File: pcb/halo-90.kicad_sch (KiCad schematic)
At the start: 111 parts, among them U1 UFQFPN28, U2 LSM6DSM

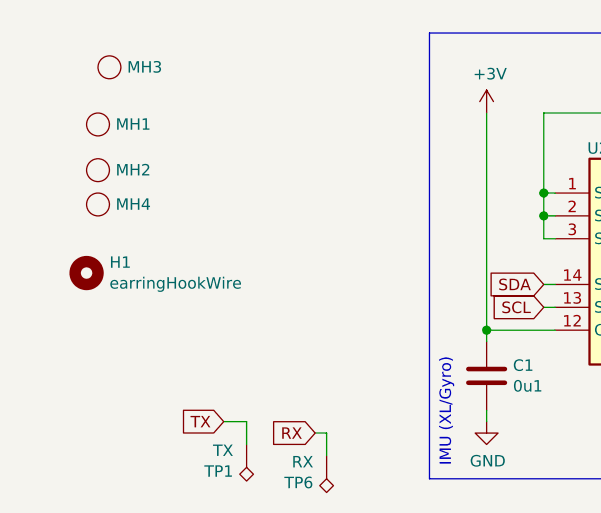
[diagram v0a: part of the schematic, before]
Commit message: Moved earwire andded to docs
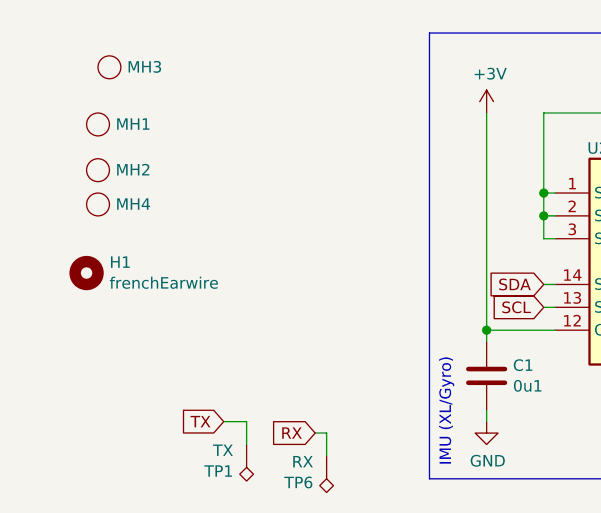
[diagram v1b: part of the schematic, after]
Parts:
- H1: value earringHookWire -> frenchEarwire; footprint earringHookWire:earringHookWire -> frenchEarwire:frenchEarwire
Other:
- title: Halo -> HALO-90

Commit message: Docs improvment
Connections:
- net RX: no longer TP6.1, U1.23 (PC2)
- net TX: no longer TP1.1, U1.24 (PC3)
- new net: TP6.1, U1.23 (PC2)
- new net: TP1.1, U1.24 (PC3)
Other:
- note added: "Chalieplex LEDs"
- note added: "Earwire"
- note added: "Microphone"
- note added: "Tooling"
- moved on the sheet: BT1, C2, H1, MH1, MH2, MH3, MH4, MK1, R1, R2, TP1, TP3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

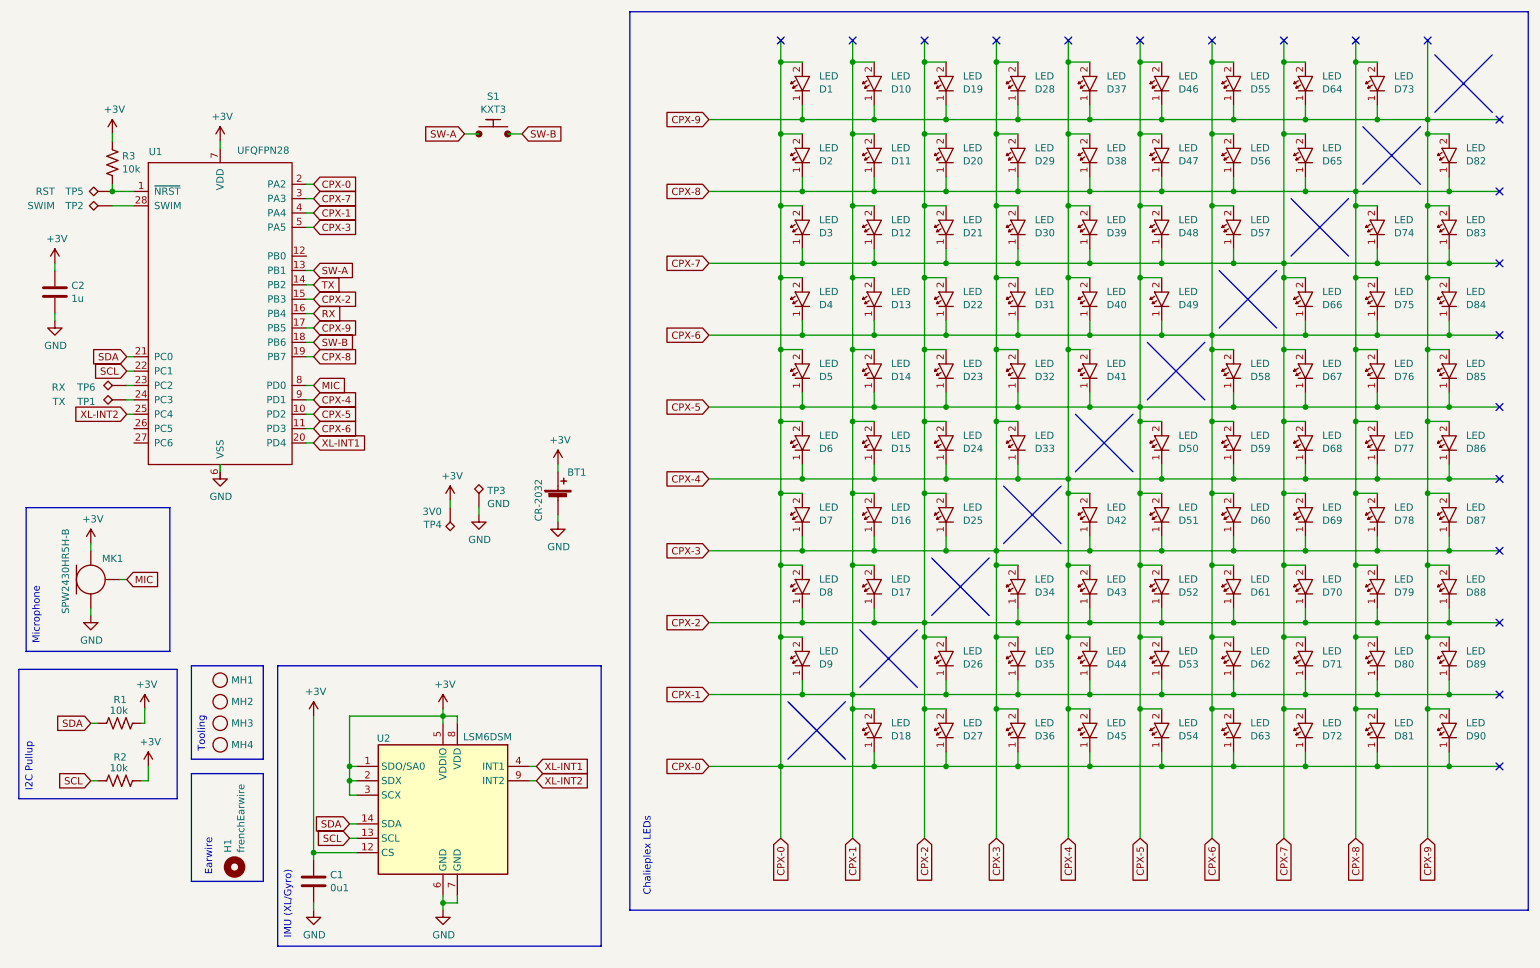
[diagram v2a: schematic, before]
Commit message: Added gifs to readme
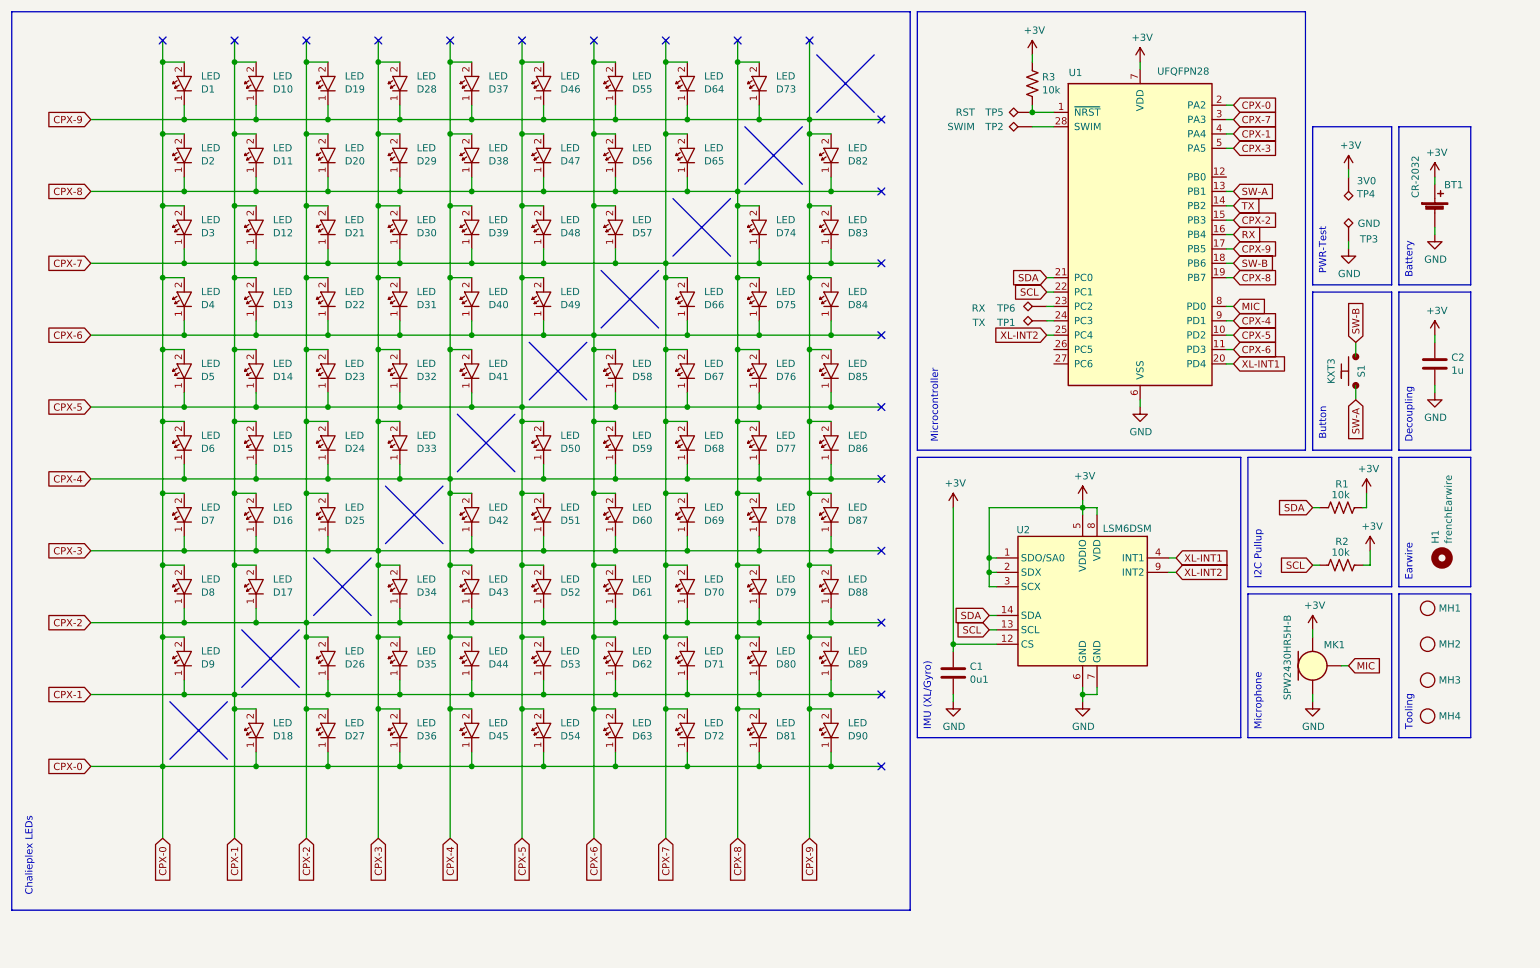
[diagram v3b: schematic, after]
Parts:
- BT1: footprint BAT-HLD-001:BAT-HLD-001-HALO -> BAT-HLD-001:BAT-HLD-001
- H1: symbol earringHookWire:earringHookWire -> frenchEarwire:frenchEarwire
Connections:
- net GND: now also U1.6 (VSS)
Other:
- note added: "Battery"
- note added: "Button"
- note added: "Decoupling"
- note added: "Microcontroller"
- note added: "PWR-Test"
- moved on the sheet: BT1, C1, C2, D1, D10, D11, D12, D13, D14, D15, D16, D17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

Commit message: Acceleometer shcematic done?
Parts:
- removed C1: 0u1, passives:C-0402, symbol passives:C-0402
- removed C2: 1u, passives:C-0402, symbol passives:C-0402
- removed H1: frenchEarwire, frenchEarwire:frenchEarwire, symbol frenchEarwire:frenchEarwire
- removed MH1, MH2, MH3, MH4: toolingHole, tooling:1.152mm-ToolingHole, symbol tooling:toolingHole
- removed MK1: SPW2430HR5H-B, SPW2430HR5H-B:SPW2430HR5H-B, symbol SPW2430HR5H-B:SPW2430HR5H-B
- removed R1, R2, R3: 10k, passives:R-0402, symbol passives:R-0402
- removed S1: KXT3, KXT3:KXT3, symbol KXT3:KXT3
- removed TP1: TX, tooling:TestPoint_Pad_D1.0mm, symbol tooling:TestPoint_D1.0
- removed TP2: SWIM, tooling:TestPoint_Pad_D1.0mm, symbol tooling:TestPoint_D1.0
- removed TP3: GND, tooling:TestPoint_Pad_D1.0mm, symbol tooling:TestPoint_D1.0
- removed TP4: 3V0, tooling:TestPoint_Pad_D1.0mm, symbol tooling:TestPoint_D1.0
- removed TP5: RST, tooling:TestPoint_Pad_D1.0mm, symbol tooling:TestPoint_D1.0
- removed TP6: RX, tooling:TestPoint_Pad_D1.0mm, symbol tooling:TestPoint_D1.0
- removed U1: UFQFPN28, STM8L15xxx:UFQFPN28, symbol STM8L15xxx:UFQFPN28
- removed U2: LSM6DSM, LSM6DSM:LGA-14_3x2.5mm_6-6, symbol LSM6DSM:LSM6DSM
- added C1, C2, C3: 100n, C-0402:C-0402, symbol C-0402:100n
- added H1: SMTSO1610MTJ, SMTSO1610MTJ:SMTSO1610MTJ, symbol SMTSO1610MTJ:SMTSO1610MTJ
- added J1: TC2030-SWIM-NL, TC2030-IDC-NL:Tag-Connect_TC2030-IDC-NL_2x03_P1.27mm_Vertical, symbol TC2030-IDC-NL:TC2030-SWIM-NL
- added R1, R2, R3: 10k, R-0402:R-0402, symbol R-0402:10k
- added U1: STM8L151xxx, STM8L15xxx:UFQFPN28, symbol STM8L15xxx:STM8L151xxx
- added U2: SC7A20HTR, SC7A20HTR:SC7A20HTR, symbol SC7A20HTR:SC7A20HTR
- added U3: DRV5032, DRV5032:DRV5032, symbol DRV5032:DRV5032
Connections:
- net +3V: now also C1.1, C2.1, C3.1, J1.1 (VCC), R1.2, R2.2, R3.1, U1.7 (VDD), U2.3 (VDDIO), U2.7 (VDD), U3.1 (VCC)
- net CPX-0: now also U1.2 (PA2)
- net CPX-1: now also U1.4 (PA4)
- net CPX-2: now also U1.15 (PB3)
- net CPX-3: now also U1.5 (PA5)
- net CPX-4: now also U1.9 (PD1)
- net CPX-5: now also U1.10 (PD2)
- net CPX-6: now also U1.11 (PD3)
- net CPX-7: now also U1.3 (PA3)
- net CPX-8: now also U1.19 (PB7)
- net CPX-9: now also U1.17 (PB5)
- net GND: now also C1.2, C2.2, C3.2, J1.5 (GND), U1.6 (VSS), U2.8 (GNDIO), U2.9 (GND), U3.3 (GND)
- net RX: now also J1.3 (RX), U1.23 (PC2)
- net SCL: now also R2.1, U1.22 (PC1), U2.12 (SCx)
- net SDA: now also R1.1, U1.21 (PC0), U2.2 (SDx)
- net TX: now also J1.2 (TX), U1.24 (PC3)
- net XL-INT1: now also U1.20 (PD4), U2.5 (INT1)
- net XL-INT2: now also U1.25 (PC4), U2.6 (INT2)
- new net HALL: U1.8 (PD0), U3.2 (OUT)
- new net SWIM: J1.4 (SWIM), U1.28 (SWIM)
- new net ~{RESET}: J1.6 (~{RESET}), R3.2, U1.1 (~{NRST})
- no-connect marks 20 -> 29
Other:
- note added: "HALL"
- note added: "Programmer"
- note removed: "Button"
- note removed: "Decoupling"
- note removed: "Microphone"
- note removed: "PWR-Test"
- note removed: "Tooling"
- moved on the sheet: BT1

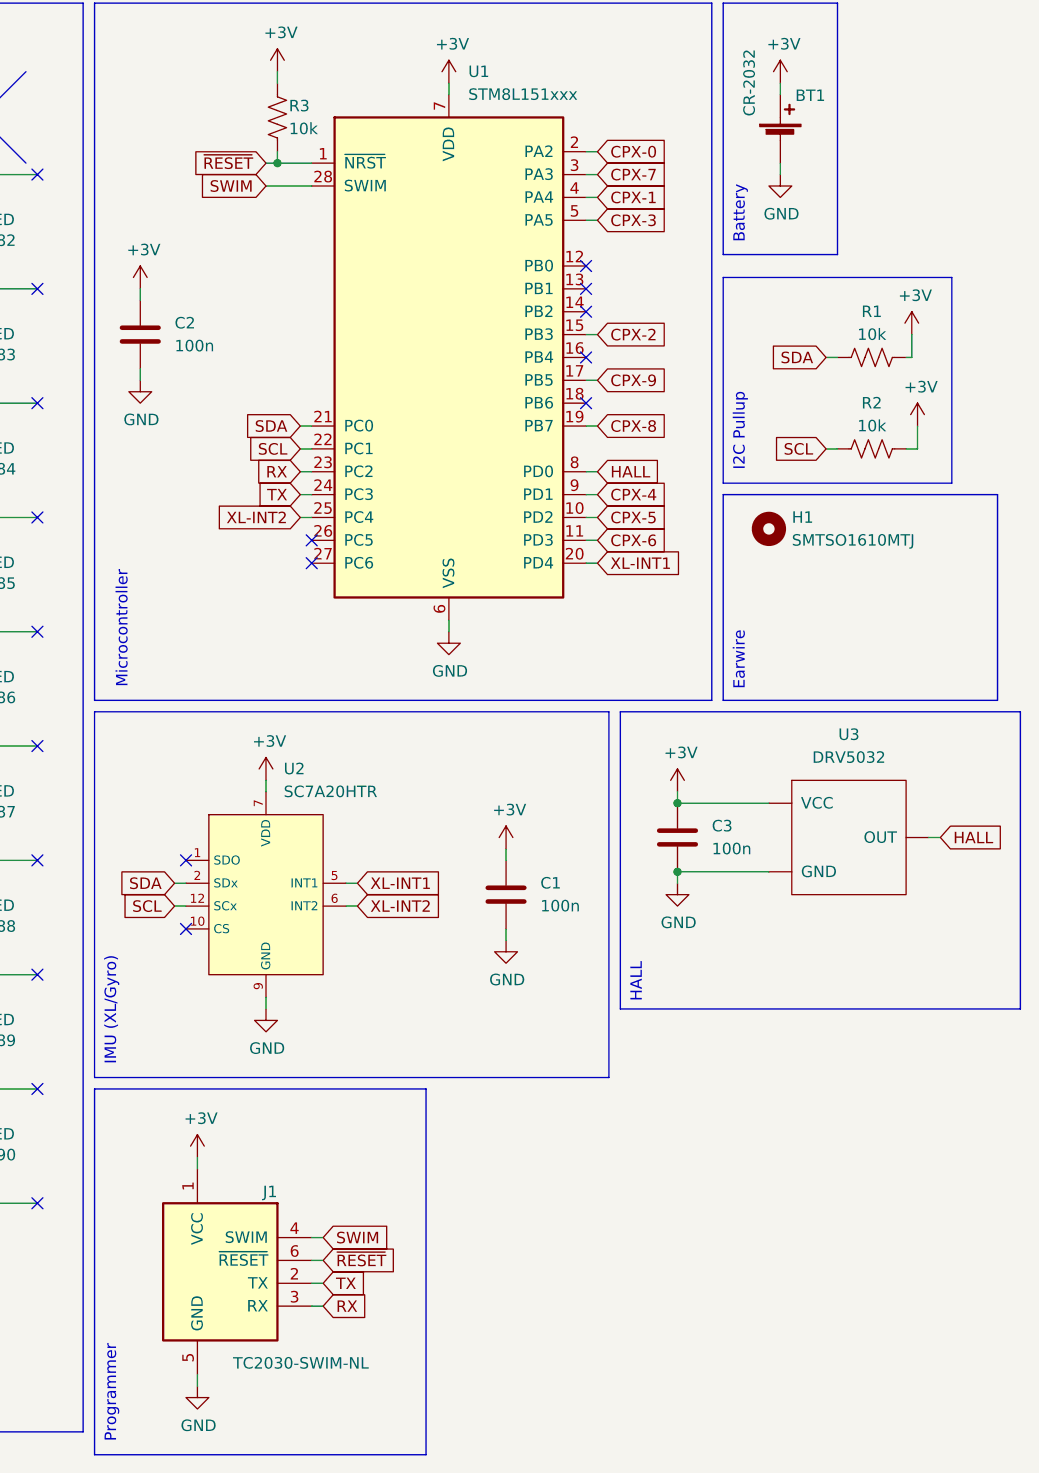
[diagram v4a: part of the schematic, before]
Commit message: updated layout, added cover
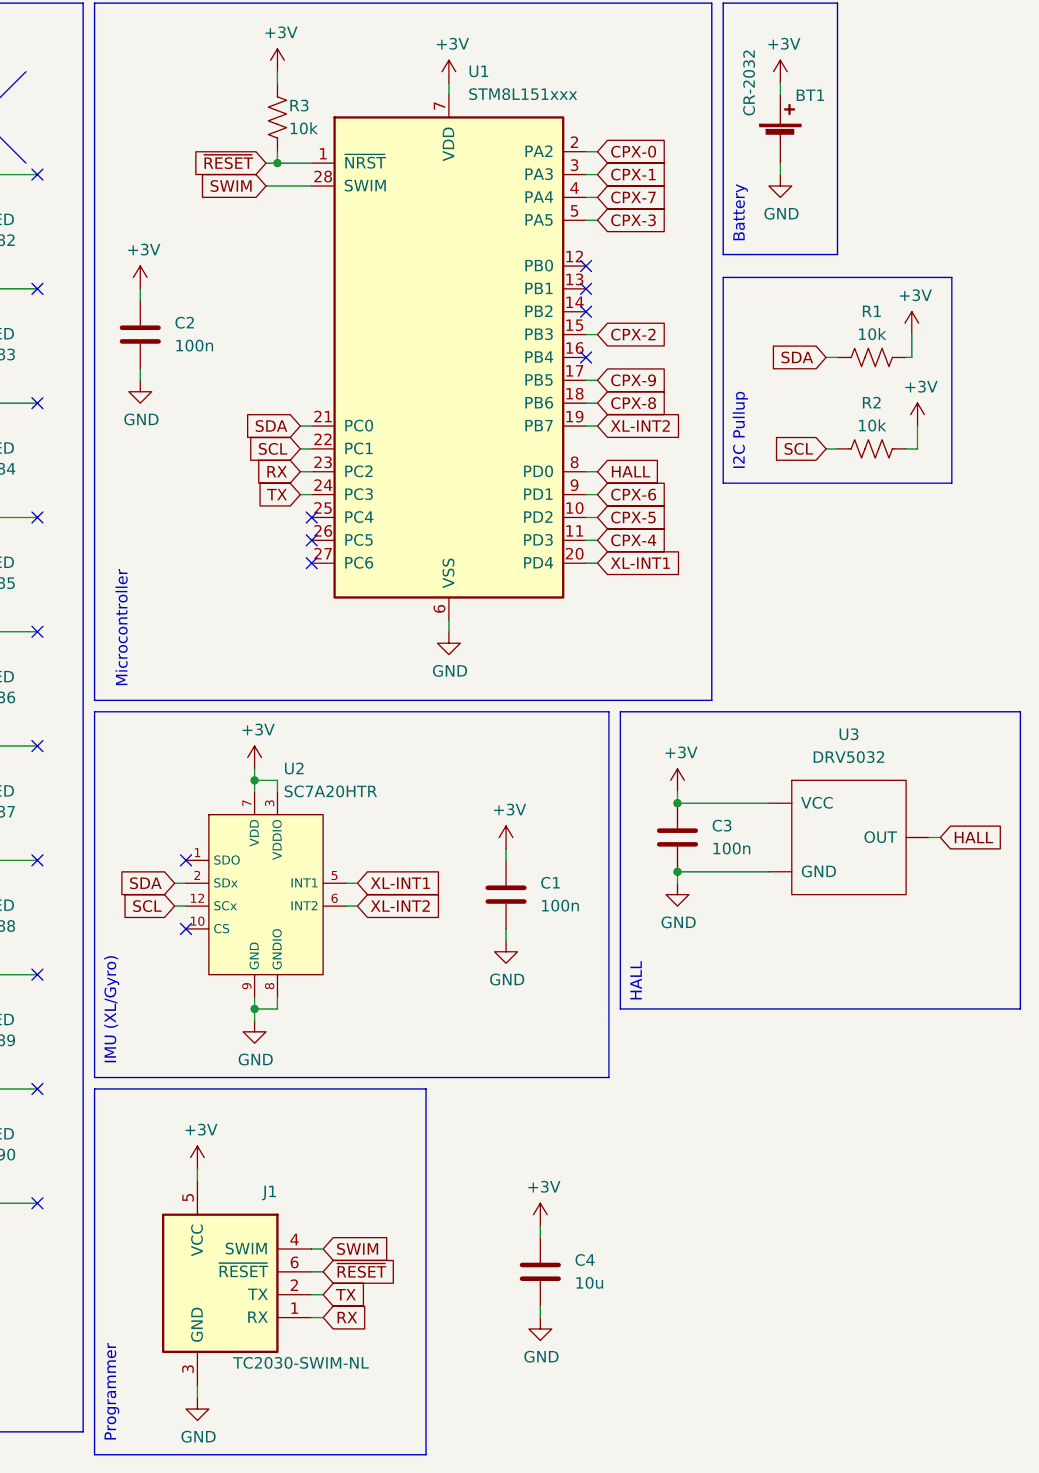
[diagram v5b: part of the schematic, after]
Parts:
- removed H1: SMTSO1610MTJ, SMTSO1610MTJ:SMTSO1610MTJ, symbol SMTSO1610MTJ:SMTSO1610MTJ
- added C4: 10u, C-0402:C-0402, symbol C-0402:10u
- U3: LCSC Part# (none) -> C2655033; MPN (none) -> DRV5032FBDBZR; Manufacturer (none) -> Texas Instruments
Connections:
- net +3V: now also J1.5 (VCC), C4.1; no longer J1.1 (VCC)
- net CPX-1: now also U1.3 (PA3); no longer U1.4 (PA4)
- net CPX-4: now also U1.11 (PD3); no longer U1.9 (PD1)
- net CPX-6: now also U1.9 (PD1); no longer U1.11 (PD3)
- net CPX-7: now also U1.4 (PA4); no longer U1.3 (PA3)
- net CPX-8: now also U1.18 (PB6); no longer U1.19 (PB7)
- net GND: now also J1.3 (GND), C4.2; no longer J1.5 (GND)
- net RX: now also J1.1 (RX); no longer J1.3 (RX)
- net XL-INT2: now also U1.19 (PB7); no longer U1.25 (PC4)
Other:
- note removed: "Earwire"
- moved on the sheet: J1

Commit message: Manufacturing: Finalize KiCad Schematics and Repackage Production Files
- Fixed 94 ERC output pin conflicts by redefining LED:BL-HUB37A symbols electrically as 'Passive'.
- Removed erroneous 'No Connect' markers from 11 actively routed STM8L GPIO pins.
- Suppressed schematic localized library mismatch warnings due to LED pin alterations.
- Deleted outdated manual 'bom.csv' in favor of the dynamic 'gerbers/BOM_JLCPCB.csv' source of truth.
- Regenerated final Gerber/Drill manufacturing files and packaged 'gerbers.zip'.
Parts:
- BT1: LCSC Part # (none) -> C7501066
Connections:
- no-connect marks 29 -> 9
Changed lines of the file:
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@@
 	)
 	(no_connect
-		(at 167.64 71.12)
-	)
-	(no_connect
 		(at 184.15 116.84)
 	)
 	(no_connect
-		(at 154.94 19.05)
-	)
-	(no_connect
-		(at 129.54 19.05)
-	)
-	(no_connect
-		(at 53.34 19.05)
-	)
-	(no_connect
 		(at 198.12 71.12)
 	)
@@
 	)
 	(no_connect
-		(at 167.64 147.32)
-	)
-	(no_connect
-		(at 40.64 19.05)
-	)
-	(no_connect
 		(at 228.6 48.26)
 	)
 	(no_connect
-		(at 116.84 19.05)
-	)
-	(no_connect
-		(at 167.64 83.82)
-	)
-	(no_connect
-		(at 104.14 19.05)
-	)
-	(no_connect
-		(at 167.64 134.62)
-	)
-	(no_connect
 		(at 228.6 43.18)
 	)
 	(no_connect
-		(at 167.64 33.02)
-	)
-	(no_connect
 		(at 228.6 45.72)
 	)
 	(no_connect
-		(at 78.74 19.05)
-	)
-	(no_connect
-		(at 167.64 58.42)
-	)
-	(no_connect
-		(at 167.64 121.92)
-	)
-	(no_connect
-		(at 66.04 19.05)
-	)
-	(no_connect
-		(at 142.24 19.05)
-	)
-	(no_connect
 		(at 198.12 73.66)
 	)
 	(no_connect
-		(at 167.64 96.52)
-	)
-	(no_connect
 		(at 198.12 76.2)
 	)
 	(no_connect
-		(at 91.44 19.05)
-	)
-	(no_connect
 		(at 184.15 109.22)
 	)
-	(no_connect
-		(at 167.64 45.72)
-	)
-	(no_connect
-		(at 167.64 109.22)
-	)
 	(wire
 		(pts
@@
 			)
 		)
+		(property "LCSC Part #" "C7501066"
+			(at 250.19 31.75 0)
+			(effects
+				(font
+					(size 1.27 1.27)
+				)
+				(hide yes)
+			)
+		)

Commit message: fix(pcb): update STM MCU, reformat BOM and PnP files
- Replaced STM8L15xxx with STM8151G6U6 in symbols, footprints, directories, and documentation
- Assigned JLCPCB part number C85325 to the new MCU in the schematic
- Scaled CPL pick & place coordinates to millimeters so JLC doesn't position everything at parsing origin
- Grouped BOM by footprint/values matching JLCPCB format
- Generated updated gerbers.zip
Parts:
- BT1: LCSC Part # C7501066 -> C85325
- C1, C2, C3: LCSC Part # C1525 -> C85325
- C4: LCSC Part # C15525 -> C85325
- R1, R3: LCSC Part # C25744 -> C85325
- U1: value STM8L151xxx -> STM8151G6U6; footprint STM8L15xxx:UFQFPN28 -> STM8151G6U6:UFQFPN28; symbol STM8L15xxx:STM8L151xxx -> STM8151G6U6:STM8151G6U6
- U2: LCSC Part # (none) -> C85325; LCSC Part# C19274408 -> (none)
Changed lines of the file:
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@@
 			)
 		)
-		(property "LCSC Part #" "C25744"
+		(property "LCSC Part #" "C85325"
 			(at 194.31 41.91 0)
 			(effects
@@
 			)
 		)
-		(property "LCSC Part #" "C1525"
+		(property "LCSC Part #" "C85325"
 			(at 219.71 128.27 0)
 			(effects
@@
 			)
 		)
-		(property "LCSC Part #" "C1525"
+		(property "LCSC Part #" "C85325"
 			(at 238.76 121.92 0)
 			(effects
@@
 			)
 		)
-		(property "LCSC Part #" "C1525"
+		(property "LCSC Part #" "C85325"
 			(at 179.07 66.04 0)
 			(effects
@@
 			)
 		)
-		(property "LCSC Part #" "C7501066"
+		(property "LCSC Part #" "C85325"
 			(at 250.19 31.75 0)
 			(effects
@@
 			)
 		)
-		(property "LCSC Part#" "C19274408"
+		(property "LCSC Part #" "C85325"
 			(at 193.04 143.51 0)
 			(effects
@@
 			)
 		)
-		(property "LCSC Part #" "C15525"
+		(property "LCSC Part #" "C85325"
 			(at 223.52 170.18 0)
 			(effects
@@
 			)
 		)
-		(property "LCSC Part #" "C25744"
+		(property "LCSC Part #" "C85325"
 			(at 275.59 53.34 0)
 			(effects
@@
 	)
 	(symbol
-		(lib_id "STM8L15xxx:STM8L151xxx")
+		(lib_id "STM8151G6U6:STM8151G6U6")
 		(at 213.36 40.64 0)
 		(unit 1)
@@
 			)
 		)
-		(property "Value" "STM8L151xxx"
+		(property "Value" "STM8151G6U6"
 			(at 215.5033 24.13 0)
 			(effects
@@
 			)
 		)
-		(property "Footprint" "STM8L15xxx:UFQFPN28"
+		(property "Footprint" "STM8151G6U6:UFQFPN28"
 			(at 213.36 92.71 0)
 			(effects
@@
 			)
 		)
-		(property "Datasheet" "${KIPRJMOD}/components/STM8L15xxx/STM8L15xxx.pdf"
+		(property "Datasheet" "${KIPRJMOD}/components/STM8151G6U6/STM8151G6U6.pdf"
 			(at 213.36 95.25 0)
 			(effects
